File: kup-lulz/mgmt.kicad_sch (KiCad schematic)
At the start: 24 parts, among them J37 XILINX_JTAG, J38 PMOD_HOST, J39 CONN_01X03, U14 STM32L431VxIx, U15 AT24MAC402, U9 XILINX_ULTRASCALEPLUS_B676

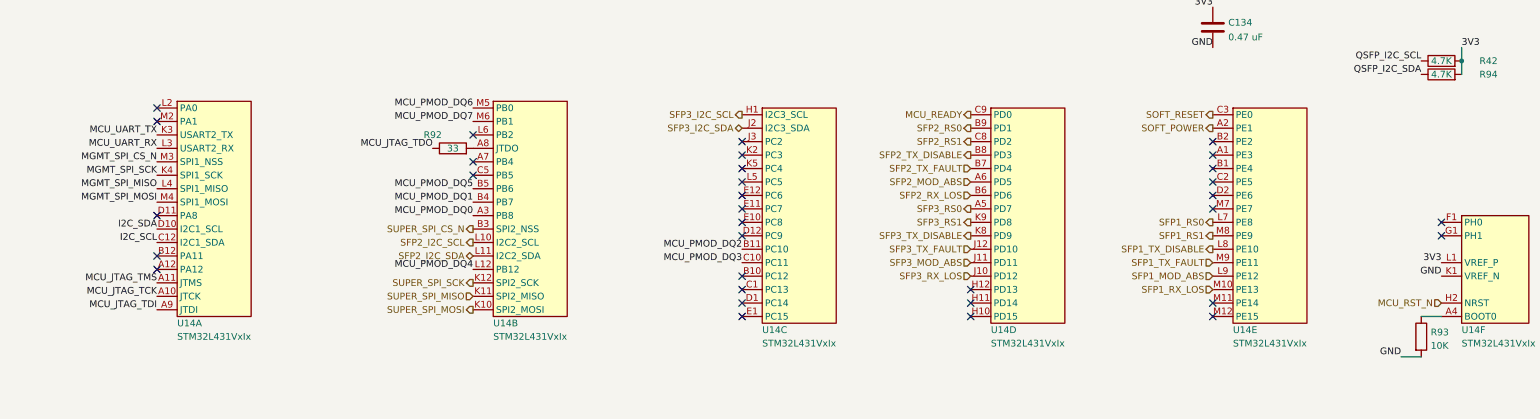
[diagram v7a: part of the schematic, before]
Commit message: Started MCU routing
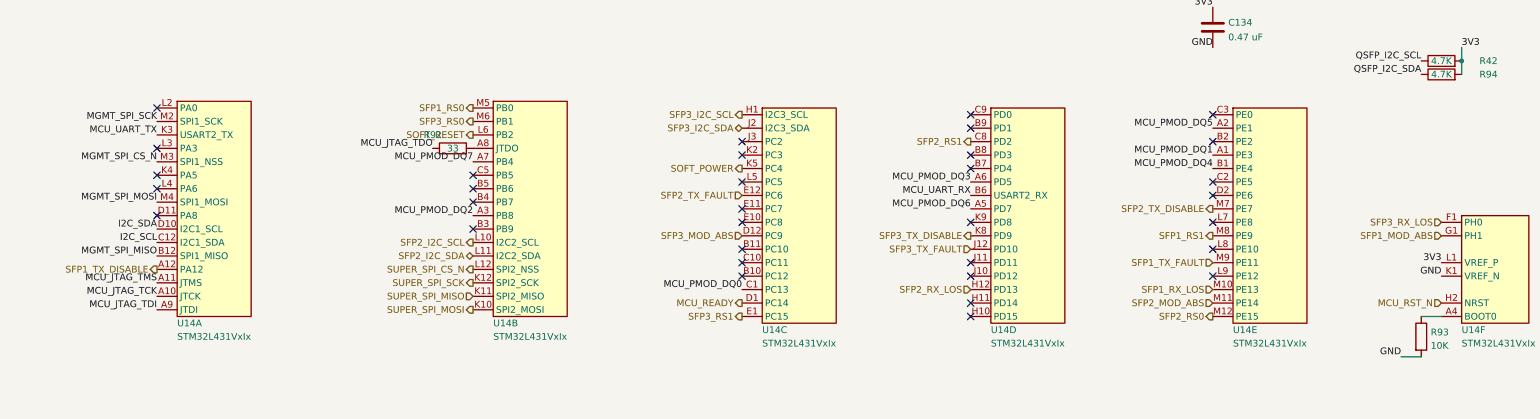
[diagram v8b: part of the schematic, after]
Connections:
- net MCU_PMOD_DQ0: now also U14.C1 (PC13); no longer U14.A3 (PB8)
- net MCU_PMOD_DQ1: now also U14.A1 (PE3); no longer U14.B4 (PB7)
- net MCU_PMOD_DQ2: now also U14.A3 (PB8); no longer U14.B11 (PC10)
- net MCU_PMOD_DQ3: now also U14.A6 (PD5); no longer U14.C10 (PC11)
- net MCU_PMOD_DQ4: now also U14.B1 (PE4); no longer U14.L12 (PB12)
- net MCU_PMOD_DQ5: now also U14.A2 (PE1); no longer U14.B5 (PB6)
- net MCU_PMOD_DQ6: now also U14.A5 (PD7); no longer U14.M5 (PB0)
- net MCU_PMOD_DQ7: now also U14.A7 (PB4); no longer U14.M6 (PB1)
- net MCU_READY: now also U14.D1 (PC14); no longer U14.C9 (PD0)
- net MCU_UART_RX: now also U14.B6 (PD6); no longer U14.L3 (PA3)
- net MGMT_SPI_MISO: now also U14.B12 (PA11); no longer U14.L4 (PA6)
- net MGMT_SPI_SCK: now also U14.M2 (PA1); no longer U14.K4 (PA5)
- net SFP1_MOD_ABS: now also U14.G1 (PH1); no longer U14.L9 (PE12)
- net SFP1_RS0: now also U14.M5 (PB0); no longer U14.L7 (PE8)
- net SFP1_TX_DISABLE: now also U14.A12 (PA12); no longer U14.L8 (PE10)
- net SFP2_MOD_ABS: now also U14.M11 (PE14); no longer U14.A6 (PD5)
- net SFP2_RS0: now also U14.M12 (PE15); no longer U14.B9 (PD1)
- net SFP2_RX_LOS: now also U14.H12 (PD13); no longer U14.B6 (PD6)
- net SFP2_TX_DISABLE: now also U14.M7 (PE7); no longer U14.B8 (PD3)
- net SFP2_TX_FAULT: now also U14.E12 (PC6); no longer U14.B7 (PD4)
- net SFP3_MOD_ABS: now also U14.D12 (PC9); no longer U14.J11 (PD11)
- net SFP3_RS0: now also U14.M6 (PB1); no longer U14.A5 (PD7)
- net SFP3_RS1: now also U14.E1 (PC15); no longer U14.K9 (PD8)
- net SFP3_RX_LOS: now also U14.F1 (PH0); no longer U14.J10 (PD12)
- net SOFT_POWER: now also U14.K5 (PC4); no longer U14.A2 (PE1)
- net SOFT_RESET: now also U14.L6 (PB2); no longer U14.C3 (PE0)
- net SUPER_SPI_CS_N: now also U14.L12 (PB12); no longer U14.B3 (PB9)
